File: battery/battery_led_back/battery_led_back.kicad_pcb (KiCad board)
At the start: 2 copper layers, 20 parts

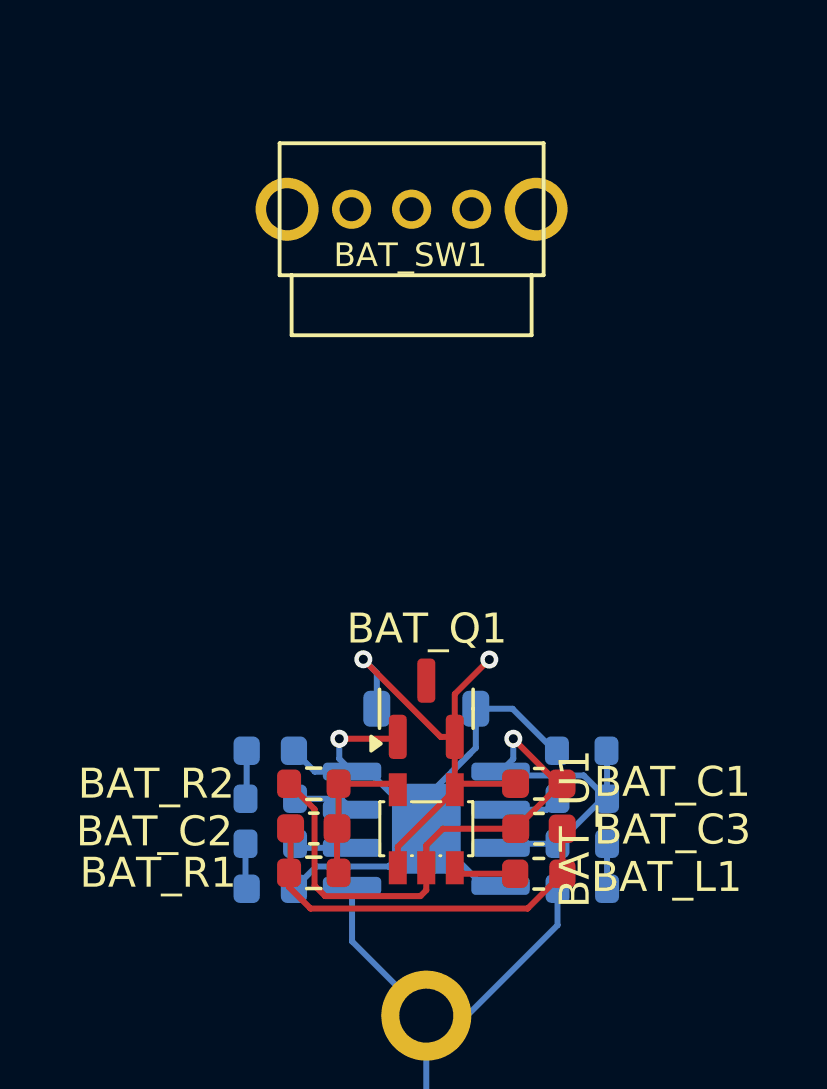
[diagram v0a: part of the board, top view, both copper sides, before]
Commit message: update battery switch symbol
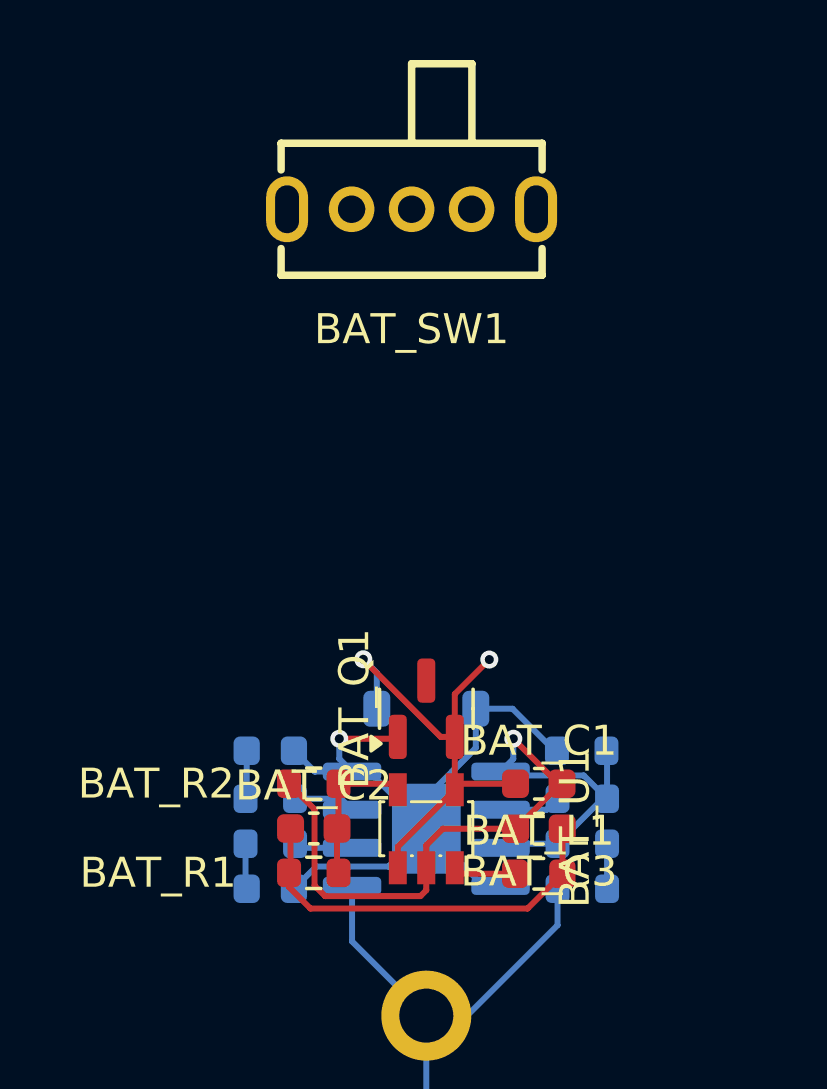
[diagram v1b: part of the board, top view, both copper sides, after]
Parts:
- BAT_C1, BAT_C2, BAT_C3: footprint ErgoCai.pretty:C_0603_1608Metric -> Capacitor_SMD:C_0603_1608Metric
- BAT_L1: footprint ErgoCai.pretty:L_0603_1608Metric -> Inductor_SMD:L_0603_1608Metric
- BAT_Q1: footprint ErgoCai.pretty:SOT-23 -> Package_TO_SOT_SMD:SOT-23
- BAT_SW1: footprint ErgoCai.pretty:SK12D07VG4 -> easyeda2kicad:SW-TH_SK12D07VG4
- BAT_TP1: footprint ErgoCai.pretty:SOIC-8-1EP_3.9x4.9mm_P1.27mm_EP2.29x3mm -> Package_SO:SOIC-8-1EP_3.9x4.9mm_P1.27mm_EP2.29x3mm
- BAT_U1: footprint ErgoCai.pretty:SOT-23-5_L3.0-W1.7-P0.95-LS2.8-BR -> easyeda2kicad:SOT-23-5_L3.0-W1.7-P0.95-LS2.8-BR
- turned BAT_SW1 to 180 degrees
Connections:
- BAT_SW1 pad 2: unconnected-(BAT_SW1-Pad2) -> VBAT

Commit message: remove default battery
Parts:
- BAT_C1, BAT_C2, BAT_C3: footprint Capacitor_SMD:C_0603_1608Metric -> ErgoCai.pretty:C_0603_1608Metric
- BAT_L1: footprint Inductor_SMD:L_0603_1608Metric -> ErgoCai.pretty:L_0603_1608Metric
- BAT_Q1: footprint Package_TO_SOT_SMD:SOT-23 -> ErgoCai.pretty:SOT-23
- BAT_SW1: footprint easyeda2kicad:SW-TH_SK12D07VG4 -> ErgoCai.pretty:SW-TH_SK12D07VG4
- BAT_TP1: footprint Package_SO:SOIC-8-1EP_3.9x4.9mm_P1.27mm_EP2.29x3mm -> ErgoCai.pretty:SOIC-8-1EP_3.9x4.9mm_P1.27mm_EP2.29x3mm
- BAT_U1: footprint easyeda2kicad:SOT-23-5_L3.0-W1.7-P0.95-LS2.8-BR -> ErgoCai.pretty:SOT-23-5_L3.0-W1.7-P0.95-LS2.8-BR
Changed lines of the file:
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@@
 	(net 14 "Net-(BAT_U1-LX)")
 	(net 15 "unconnected-(BAT_SW1-Pad3)")
-	(footprint "easyeda2kicad:SOT-23-5_L3.0-W1.7-P0.95-LS2.8-BR"
+	(footprint "ErgoCai.pretty:SOT-23-5_L3.0-W1.7-P0.95-LS2.8-BR"
 		(layer "F.Cu")
 		(at 0 -38 -90)
@@
 			(layer "Cmts.User")
 		)
+		(fp_line
+			(start -2.05 1.7)
+			(end 2.05 1.7)
+			(stroke
+				(width 0.05)
+				(type solid)
+			)
+			(layer "F.CrtYd")
+		)
+		(fp_line
+			(start 2.05 1.7)
+			(end 2.05 -1.7)
+			(stroke
+				(width 0.05)
+				(type solid)
+			)
+			(layer "F.CrtYd")
+		)
+		(fp_line
+			(start -2.05 -1.7)
+			(end -2.05 1.7)
+			(stroke
+				(width 0.05)
+				(type solid)
+			)
+			(layer "F.CrtYd")
+		)
+		(fp_line
+			(start 2.05 -1.7)
+			(end -2.05 -1.7)
+			(stroke
+				(width 0.05)
+				(type solid)
+			)
+			(layer "F.CrtYd")
+		)
 		(fp_circle
 			(center 1.4 1.45)
@@
 		)
 		(embedded_fonts no)
-		(model "${EASYEDA2KICAD}/easyeda2kicad.3dshapes/SOT-23-5_L2.9-W1.6-H1.1-LS2.8-P0.95.wrl"
+		(model "/Users/jinsongc/Development/ErgoCaiLib/3dmodels/SOT-23-5_L2.9-W1.6-H1.1-LS2.8-P0.95.wrl"
 			(offset
 				(xyz 0 -0 -0)
@@
 		)
 	)
-	(footprint "Inductor_SMD:L_0603_1608Metric"
+	(footprint "ErgoCai.pretty:L_0603_1608Metric"
 		(layer "F.Cu")
 		(at 3.75 -36.5)
@@
 		)
 	)
-	(footprint "Package_TO_SOT_SMD:SOT-23"
+	(footprint "ErgoCai.pretty:SOT-23"
 		(layer "F.Cu")
 		(at 0 -42 90)
-		(descr "SOT, 3 Pin (JEDEC TO-236 Var AB https://www.jedec.org/document_search?search_api_views_fulltext=TO-236), generated with kicad-footprint-generator ipc_gullwing_generator.py")
+		(descr "SOT, 3 Pin (https://www.jedec.org/system/files/docs/to-236h.pdf variant AB), generated with kicad-footprint-generator ipc_gullwing_generator.py")
 		(tags "SOT TO_SOT_SMD")
 		(property "Reference" "BAT_Q1"
@@
 		(property "Datasheet" "http://www.aosmd.com/pdfs/datasheet/AO3401A.pdf"
 			(at 0 0 90)
+			(unlocked yes)
 			(layer "F.Fab")
 			(hide yes)
@@
 		(property "Description" "-4.0A Id, -30V Vds, P-Channel MOSFET, SOT-23"
 			(at 0 0 90)
+			(unlocked yes)
 			(layer "F.Fab")
 			(hide yes)
@@
 		(fp_poly
 			(pts
-				(xy -1.1625 -1.51) (xy -1.4025 -1.84) (xy -0.9225 -1.84)
+				(xy -1.1625 -1.51) (xy -1.4025 -1.84) (xy -0.9225 -1.84) (xy -1.1625 -1.51)
 			)
 			(stroke
@@
 		)
 		(fp_line
-			(start 0.9 -1.7)
-			(end 0.9 -0.55)
-			(stroke
-				(width 0.05)
-				(type solid)
-			)
-			(layer "F.CrtYd")
-		)
-		(fp_line
-			(start -0.9 -1.7)
-			(end 0.9 -1.7)
+			(start 1.92 -1.7)
+			(end -1.92 -1.7)
 			(stroke
 				(width 0.05)
@@
 		)
 		(fp_line
-			(start -0.9 -1.5)
-			(end -0.9 -1.7)
+			(start -1.92 -1.7)
+			(end -1.92 1.7)
 			(stroke
 				(width 0.05)
@@
 		)
 		(fp_line
-			(start -1.93 -1.5)
-			(end -0.9 -1.5)
+			(start 1.92 1.7)
+			(end 1.92 -1.7)
 			(stroke
 				(width 0.05)
@@
 		)
 		(fp_line
-			(start 1.93 -0.55)
-			(end 1.93 0.55)
+			(start -1.92 1.7)
+			(end 1.92 1.7)
 			(stroke
 				(width 0.05)
@@
 		)
 		(fp_line
-			(start 0.9 -0.55)
-			(end 1.93 -0.55)
+			(start 0.65 -1.45)
+			(end 0.65 1.45)
 			(stroke
-				(width 0.05)
-				(type solid)
-			)
-			(layer "F.CrtYd")
-		)
-		(fp_line
-			(start 1.93 0.55)
-			(end 0.9 0.55)
-			(stroke
-				(width 0.05)
-				(type solid)
-			)
-			(layer "F.CrtYd")
-		)
-		(fp_line
-			(start 0.9 0.55)
-			(end 0.9 1.7)
-			(stroke
-				(width 0.05)
+				(width 0.1)
 				(type solid)
 			)
-			(layer "F.CrtYd")
+			(layer "F.Fab")
 		)
 		(fp_line
-			(start -0.9 1.5)
-			(end -1.93 1.5)
+			(start -0.325 -1.45)
+			(end 0.65 -1.45)
 			(stroke
-				(width 0.05)
+				(width 0.1)
 				(type solid)
 			)
-			(layer "F.CrtYd")
+			(layer "F.Fab")
 		)
 		(fp_line
-			(start -1.93 1.5)
-			(end -1.93 -1.5)
+			(start -0.65 -1.125)
+			(end -0.325 -1.45)
 			(stroke
-				(width 0.05)
+				(width 0.1)
 				(type solid)
 			)
-			(layer "F.CrtYd")
+			(layer "F.Fab")
 		)
 		(fp_line
-			(start 0.9 1.7)
-			(end -0.9 1.7)
+			(start 0.65 1.45)
+			(end -0.65 1.45)
 			(stroke
-				(width 0.05)
+				(width 0.1)
 				(type solid)
 			)
-			(layer "F.CrtYd")
+			(layer "F.Fab")
 		)
 		(fp_line
-			(start -0.9 1.7)
-			(end -0.9 1.5)
-			(stroke
-				(width 0.05)
-				(type solid)
-			)
-			(layer "F.CrtYd")
-		)
-		(fp_poly
-			(pts
-				(xy -0.65 -1.125) (xy -0.65 1.45) (xy 0.65 1.45) (xy 0.65 -1.45) (xy -0.325 -1.45)
-			)
+			(start -0.65 1.45)
+			(end -0.65 -1.125)
 			(stroke
 				(width 0.1)
 				(type solid)
 			)
-			(fill no)
 			(layer "F.Fab")
 		)
@@
 		)
 		(embedded_fonts no)
-		(model "${KICAD9_3DMODEL_DIR}/Package_TO_SOT_SMD.3dshapes/SOT-23.step"
+		(model "${KICAD8_3DMODEL_DIR}/Package_TO_SOT_SMD.3dshapes/SOT-23.wrl"
 			(offset
 				(xyz 0 0 0)
@@
 		)
 	)
-	(footprint "Capacitor_SMD:C_0603_1608Metric"
+	(footprint "ErgoCai.pretty:C_0603_1608Metric"
 		(layer "F.Cu")
 		(at -3.75 -38.01)
@@
 		)
 	)
-	(footprint "Capacitor_SMD:C_0603_1608Metric"
+	(footprint "ErgoCai.pretty:C_0603_1608Metric"
 		(layer "F.Cu")
 		(at 3.755 -38 180)
@@
 		)
 	)
-	(footprint "easyeda2kicad:SW-TH_SK12D07VG4"
+	(footprint "ErgoCai.pretty:SW-TH_SK12D07VG4"
 		(layer "F.Cu")
 		(at -0.49 -58.65 180)
 		(property "Reference" "BAT_SW1"
-			(at 0 -4 0)
+			(at 0 -4 180)
 			(layer "F.SilkS")
 			(effects
@@
 		)
 		(property "Value" "~"
-			(at 0 4 0)
+			(at 0 4 180)
 			(layer "F.Fab")
 			(effects
@@
 		)
 		(property "Datasheet" "https://lcsc.com/product-detail/Toggle-Switches_SHOU-HAN-SK12D07VG4_C393937.html"
-			(at 0 0 0)
+			(at 0 0 180)
 			(layer "F.Fab")
 			(hide yes)
@@
 		)
 		(property "Description" "Switch, dual pole double throw, separate symbols"
-			(at 0 0 0)
+			(at 0 0 180)
 			(layer "F.Fab")
 			(hide yes)
@@
 		)
 		(fp_text user "${REFERENCE}"
-			(at 0 0 0)
+			(at 0 0 180)
 			(layer "F.Fab")
 			(effects
@@
 		)
 	)
-	(footprint "Capacitor_SMD:C_0603_1608Metric"
+	(footprint "ErgoCai.pretty:C_0603_1608Metric"
 		(layer "F.Cu")
 		(at 3.75 -39.5)
@@
 		)
 	)
-	(footprint "Package_SO:SOIC-8-1EP_3.9x4.9mm_P1.27mm_EP2.29x3mm"
+	(footprint "ErgoCai.pretty:SOIC-8-1EP_3.9x4.9mm_P1.27mm_EP2.29x3mm"
 		(layer "B.Cu")
 		(at 0 -38 180)
@@
 		(property "Datasheet" ""
 			(at 0 0 0)
+			(unlocked yes)
 			(layer "B.Fab")
 			(hide yes)
@@
 		(property "Description" "TP4056"
 			(at 0 0 0)
+			(unlocked yes)
 			(layer "B.Fab")
 			(hide yes)
@@
 		(fp_poly
 			(pts
-				(xy -2.7 2.465) (xy -2.94 2.795) (xy -2.46 2.795)
+				(xy -2.7 2.465) (xy -2.94 2.795) (xy -2.46 2.795) (xy -2.7 2.465)
 			)
 			(stroke
@@
 		)
 		(fp_line
-			(start 3.7 2.46)
-			(end 3.7 -2.46)
-			(stroke
-				(width 0.05)
-				(type solid)
-			)
-			(layer "B.CrtYd")
-		)
-		(fp_line
-			(start 3.7 -2.46)
-			(end 2.2 -2.46)
-			(stroke
-				(width 0.05)
-				(type solid)
-			)
-			(layer "B.CrtYd")
-		)
-		(fp_line
-			(start 2.2 2.7)
-			(end 2.2 2.46)
+			(start 3.7 2.7)
+			(end -3.7 2.7)
 			(stroke
 				(width 0.05)
@@
 		)
 		(fp_line
-			(start 2.2 2.46)
-			(end 3.7 2.46)
+			(start 3.7 -2.7)
+			(end 3.7 2.7)
 			(stroke
 				(width 0.05)
@@
 		)
 		(fp_line
-			(start 2.2 -2.46)
-			(end 2.2 -2.7)
+			(start -3.7 2.7)
+			(end -3.7 -2.7)
 			(stroke
 				(width 0.05)
@@
 		)
 		(fp_line
-			(start 2.2 -2.7)
-			(end -2.2 -2.7)
+			(start -3.7 -2.7)
+			(end 3.7 -2.7)
 			(stroke
 				(width 0.05)
@@
 		)
 		(fp_line
-			(start -2.2 2.7)
-			(end 2.2 2.7)
+			(start 1.95 2.45)
+			(end 1.95 -2.45)
 			(stroke
-				(width 0.05)
-				(type solid)
-			)
-			(layer "B.CrtYd")
-		)
-		(fp_line
-			(start -2.2 2.46)
-			(end -2.2 2.7)
-			(stroke
-				(width 0.05)
+				(width 0.1)
 				(type solid)
 			)
-			(layer "B.CrtYd")
+			(layer "B.Fab")
 		)
 		(fp_line
-			(start -2.2 -2.46)
-			(end -3.7 -2.46)
+			(start 1.95 -2.45)
+			(end -1.95 -2.45)
 			(stroke
-				(width 0.05)
+				(width 0.1)
 				(type solid)
 			)
-			(layer "B.CrtYd")
+			(layer "B.Fab")
 		)
 		(fp_line
-			(start -2.2 -2.7)
-			(end -2.2 -2.46)
+			(start -0.975 2.45)
+			(end 1.95 2.45)
 			(stroke
-				(width 0.05)
+				(width 0.1)
 				(type solid)
 			)
-			(layer "B.CrtYd")
+			(layer "B.Fab")
 		)
 		(fp_line
-			(start -3.7 2.46)
-			(end -2.2 2.46)
+			(start -1.95 1.475)
+			(end -0.975 2.45)
 			(stroke
-				(width 0.05)
+				(width 0.1)
 				(type solid)
 			)
-			(layer "B.CrtYd")
+			(layer "B.Fab")
 		)
 		(fp_line
-			(start -3.7 -2.46)
-			(end -3.7 2.46)
-			(stroke
-				(width 0.05)
-				(type solid)
-			)
-			(layer "B.CrtYd")
-		)
-		(fp_poly
-			(pts
-				(xy -1.95 1.475) (xy -1.95 -2.45) (xy 1.95 -2.45) (xy 1.95 2.45) (xy -0.975 2.45)
-			)
+			(start -1.95 -2.45)
+			(end -1.95 1.475)
 			(stroke
 				(width 0.1)
 				(type solid)
 			)
-			(fill no)
 			(layer "B.Fab")
 		)
@@
 		)
 		(embedded_fonts no)
-		(model "${KICAD9_3DMODEL_DIR}/Package_SO.3dshapes/SOIC-8-1EP_3.9x4.9mm_P1.27mm_EP2.29x3mm.step"
+		(model "${KICAD8_3DMODEL_DIR}/Package_SO.3dshapes/SOIC-8-1EP_3.9x4.9mm_P1.27mm_EP2.29x3mm.wrl"
 			(offset
 				(xyz 0 0 0)

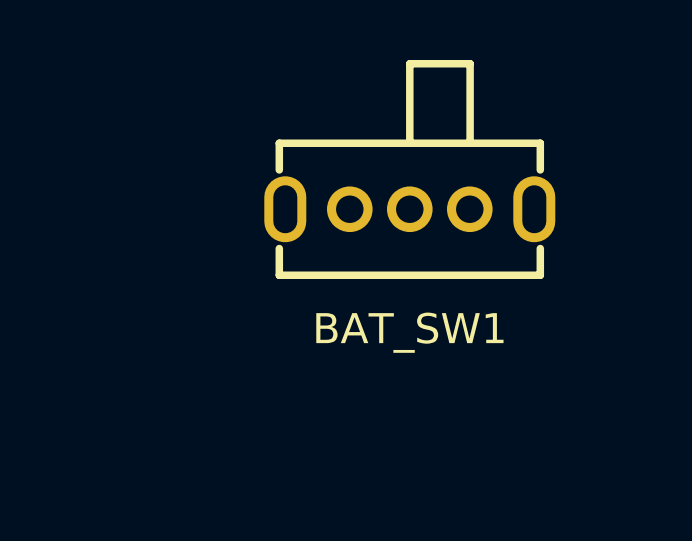
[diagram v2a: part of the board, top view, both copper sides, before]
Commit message: add power switch
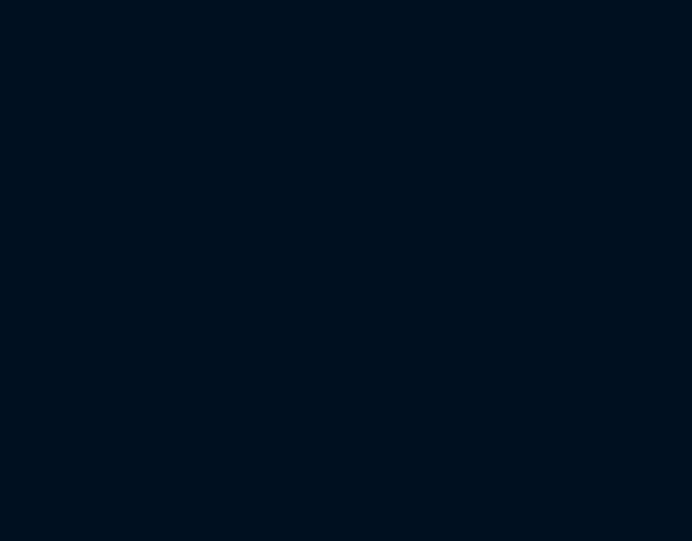
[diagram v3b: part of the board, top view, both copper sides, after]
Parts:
- removed BAT_R_PRG1: 1.2K, ErgoCai.pretty:R_0603_1608Metric
- removed BAT_SW1: ~, ErgoCai.pretty:SW-TH_SK12D07VG4
- added BAT_R_P1: 1.2K, ErgoCai.pretty:R_0603_1608Metric, B.Cu at (5.20, -39.0)
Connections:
- BAT_Q1 pad 3: Net-(BAT_Q1-D) -> VSYS

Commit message: update to 3.3V tag
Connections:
- net VCC renamed 3.3V
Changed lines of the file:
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@@
 	(net 1 "VBAT")
 	(net 2 "GND")
-	(net 3 "VCC")
+	(net 3 "3.3V")
 	(net 4 "VBUS")
 	(net 5 "ADC_BT")
@@
 			(layers "F.Cu" "F.Mask" "F.Paste")
 			(roundrect_rratio 0.25)
-			(net 3 "VCC")
+			(net 3 "3.3V")
 			(pinfunction "2")
 			(pintype "passive")
@@
 			(layers "F.Cu" "F.Mask" "F.Paste")
 			(roundrect_rratio 0.25)
-			(net 3 "VCC")
+			(net 3 "3.3V")
 			(pintype "passive")
 		)
@@
 			(layers "F.Cu" "F.Mask" "F.Paste")
 			(roundrect_rratio 0.25)
-			(net 3 "VCC")
+			(net 3 "3.3V")
 			(pintype "passive")
 		)
@@
 			(layers "F.Cu" "F.Mask" "F.Paste")
 			(roundrect_rratio 0.25)
-			(net 3 "VCC")
+			(net 3 "3.3V")
 			(pintype "passive")
 		)
